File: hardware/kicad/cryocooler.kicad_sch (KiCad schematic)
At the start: 16 parts, among them J1 USB_C, SW1 RESET, SW2 BOOT, U1 ESP32-S3-WROOM-2-N32R16V, U2 USBLC6-2SC6

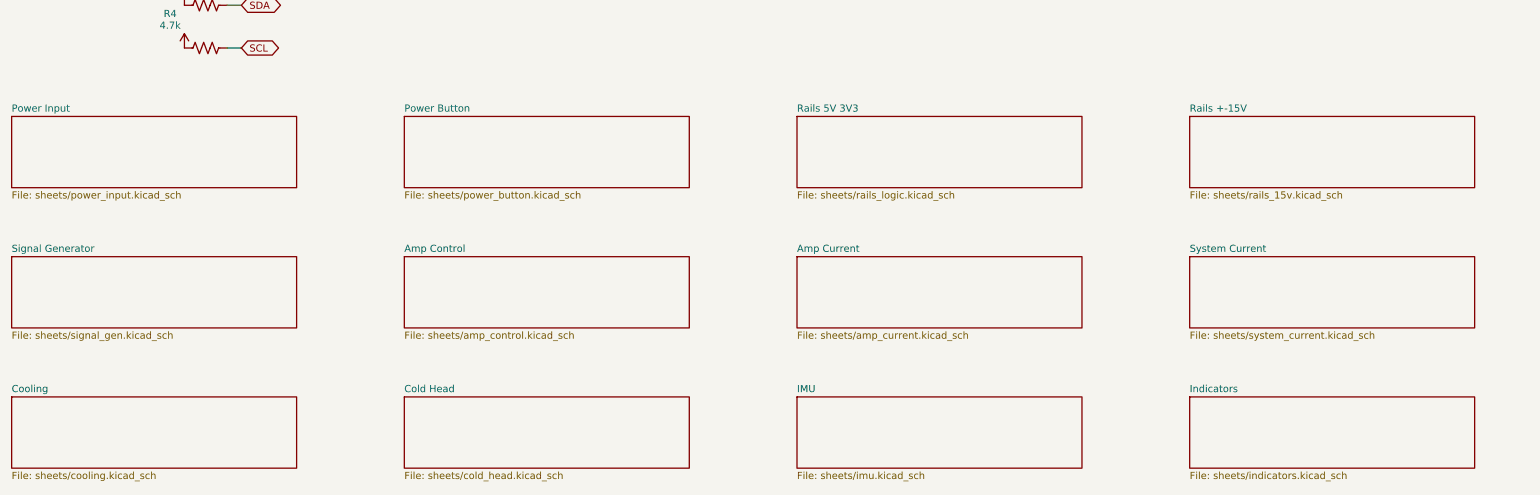
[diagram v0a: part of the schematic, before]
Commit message: Fixing the UUID issues
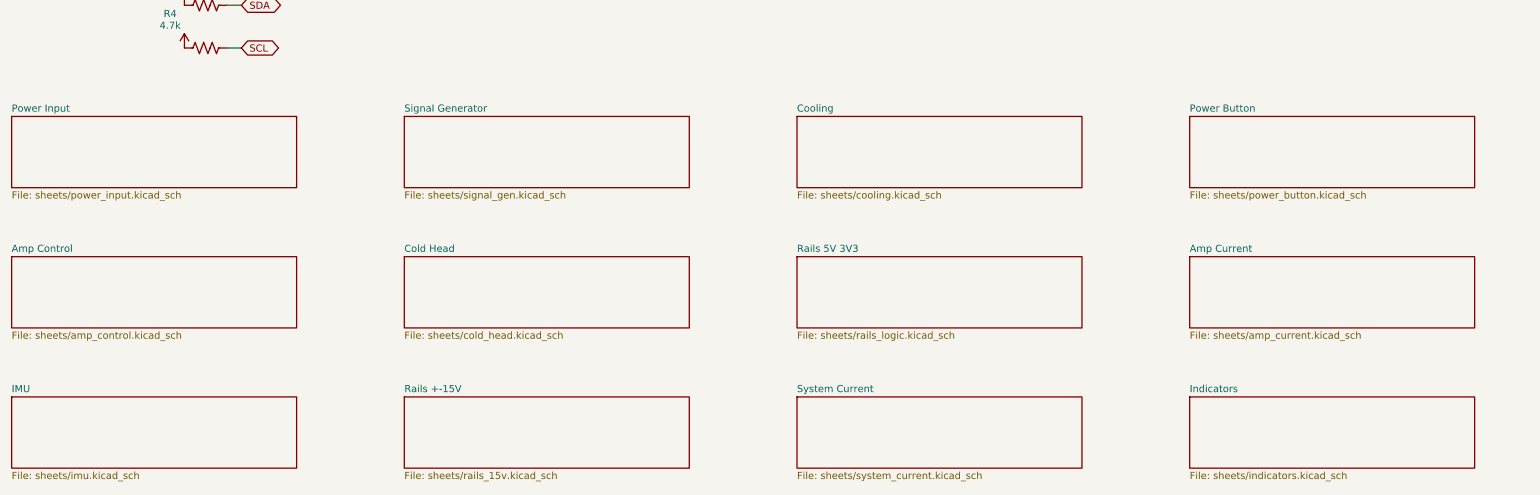
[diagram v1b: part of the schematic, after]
